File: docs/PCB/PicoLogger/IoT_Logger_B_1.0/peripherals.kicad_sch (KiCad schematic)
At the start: 71 parts, among them Q3 BC817-40-DIO, Q4 BSS138, SW3 Tact Switch 6x6mm / 13mm, SW4 Tact Switch 6x6mm / 13mm, U4 PCA9306DCUR, U5 SN65HVD230DR, U6 MCP7940N-I/SN, U8 FM24CL16B-GTR, U9 MX25L25673GM2I-08G, Y3 QT3CD-32.768KEZY-T

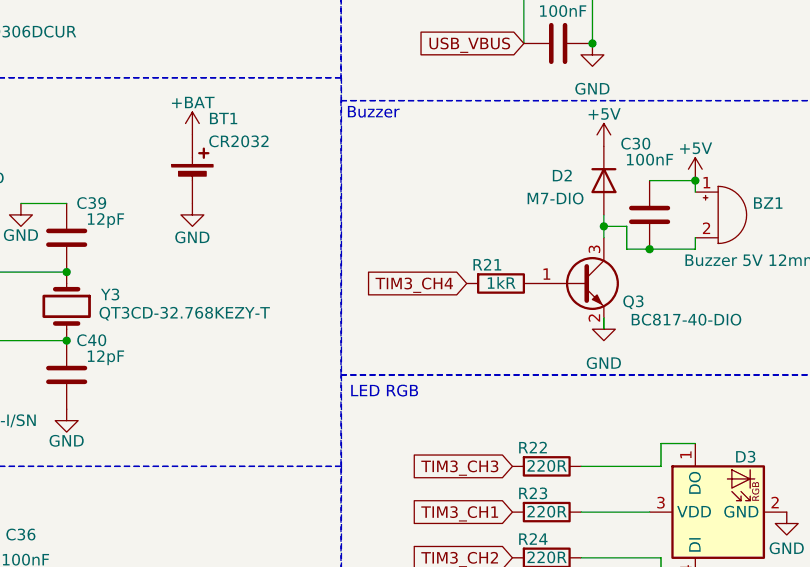
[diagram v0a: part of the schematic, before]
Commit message: HAL and LL prototypes added.
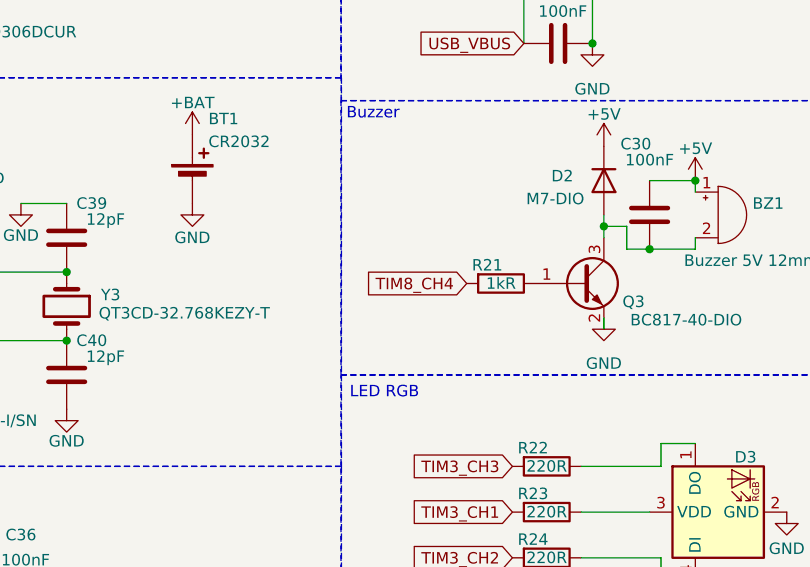
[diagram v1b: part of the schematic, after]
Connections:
- net TIM3_CH4 renamed TIM8_CH4
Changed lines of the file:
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@@
 		)
 	)
-	(global_label "TIM3_CH4"
+	(global_label "TIM8_CH4"
 		(shape input)
 		(at 104.14 78.74 180)
